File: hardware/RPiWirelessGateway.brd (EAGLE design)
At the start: 49.5 x 49.5 mm, 55 parts, among them IC1 MCP1702-3.3, X1 P1A, X2 CONN-SMATHD-SMD-EDGE, X3 P1B, X4 AVR ISP, X5 RPI FTDI

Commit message: Adding resistor to XBee TX line to protect if FTDI also fitted simultaneously.
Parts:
- added R3: 2k2, SteveMarple:RES-AXIAL-0.4
- R1: value 100k -> 1k
- R2: value 1k -> 100k
- RF2: value XRFB1 -> XRF
- X2: value CONN-SMATHD-SMD-EDGE -> SMA TH/EDGE
- moved R1 31.4 mm to (34.3, 34.3), turned to 180 degrees
- moved R2 31.4 mm to (17.8, 7.62), turned to 270 degrees
- moved U$24 24.8 mm to (21.0, 25.4), turned to 180 degrees
- moved U$11 24.8 mm to (5.08, 34.3), turned to 0 degrees
- moved U$17 22.9 mm to (5.08, 39.4), turned to 0 degrees
- moved U$25 21.6 mm to (5.71, 25.4), turned to 180 degrees
- moved U$21 19.6 mm to (21.0, 22.9), turned to 180 degrees
- moved U$14 19.1 mm to (5.08, 36.8), turned to 0 degrees
- moved U$22 19.1 mm to (5.71, 22.9), turned to 180 degrees
- moved U$20 16.5 mm to (5.08, 41.9), turned to 0 degrees
- moved U$19 16.1 mm to (5.71, 20.3)
- moved U$13 15.5 mm to (5.71, 15.2)
- moved U$18 15.5 mm to (21.0, 20.3)
- moved U$12 15.2 mm to (21.0, 15.2)
- moved U$26 10.2 mm to (5.08, 47.0)
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- renumbered XRF1 to RF2
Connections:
- new net N$42: R3.P$2, RF2.2, U$3.1
- net !XRF_RESET: now also R2.P$1; no longer R1.P$1
- net +3V3: now also R2.P$2; no longer R1.P$2
- net GND: now also U$24.1, U$26.1; no longer U$19.1, U$25.1
- net N$10: now also U$22.1; no longer U$18.1
- net N$11: now also U$19.1; no longer U$16.1
- net N$12: now also U$16.1; no longer U$14.1
- net N$13: now also U$13.1; no longer U$12.1
- net N$24: now also R1.P$2; no longer R2.P$2
- net N$30: now also U$23.1; no longer U$24.1
- net N$31: now also U$20.1; no longer U$22.1
- net N$38: now also R1.P$1; no longer R2.P$1
- net N$40: now also U$11.1; no longer U$21.1
- net N$5: now also U$12.1; no longer U$11.1
- net N$6: now also U$15.1; no longer U$13.1
- net N$7: now also U$18.1; no longer U$15.1
- net N$8: now also U$21.1; no longer U$17.1
- net N$9: now also U$25.1; no longer U$20.1
- net RX: now also U$17.1; no longer U$23.1
- net TX: now also R3.P$1, U$14.1; no longer RF2.2, U$26.1, U$3.1
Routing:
- net N$42: track 0.00 -> 12.8 mm
- net TX: track 72.4 -> 62.9 mm
- net RX: track 79.3 -> 84.2 mm
- net N$21: track 15.6 -> 12.6 mm
- net GND: track 149.9 -> 147.3 mm
- net N$22: track 10.8 -> 9.33 mm
- net N$9: track 7.85 -> 6.36 mm
- net N$20: track 10.3 -> 9.53 mm
- net P1-13: track 21.7 -> 22.4 mm
- net +3V3: track 104.6 -> 103.9 mm
- net N$41: track 17.7 -> 17.2 mm
- removed copper zone on layer 1, net +3V3

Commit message: Adding FET for open-drain control of AVR /RESET
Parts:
- added PAD_RFM12B_!INT!/VDI1, PAD_RFM12B_!INT!/VDI2: PAD, SteveMarple:PAD
- added Q1: 2N7000, SteveMarple:TO-92
- added R4: 2k2, SteveMarple:RES-AXIAL-0.4
- R1: value 1k -> 100k
- R3: value 2k2 -> 100k
- X4: device adafruit:AVRISP -> SteveMarple:CONN-HARTING-ML6
- moved U$11 24.8 mm to (21.0, 15.2), turned to 180 degrees
- moved U$15 22.9 mm to (5.08, 34.3), turned to 0 degrees
- moved U$18 22.9 mm to (5.08, 36.8), turned to 0 degrees
- moved U$21 22.9 mm to (5.08, 39.4), turned to 0 degrees
- moved U$24 22.9 mm to (5.08, 41.9), turned to 0 degrees
- moved PAD_RFM12B_FSK/DATA/!FFS 22.6 mm to (38.1, 8.89)
- moved R1 20.8 mm to (17.8, 21.6), turned to 90 degrees
- moved U$23 19.1 mm to (5.71, 25.4), turned to 180 degrees
- moved U$25 19.1 mm to (5.08, 44.5), turned to 0 degrees
- moved U$14 19.1 mm to (5.71, 17.8), turned to 180 degrees
- moved U$17 19.1 mm to (5.71, 20.3), turned to 180 degrees
- moved U$20 19.1 mm to (5.71, 22.9), turned to 180 degrees
- moved U$13 15.5 mm to (21.0, 17.8)
- moved U$16 15.5 mm to (21.0, 20.3)
- moved U$19 15.5 mm to (21.0, 22.9)
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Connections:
- net !XRF_RESET: now also R3.P$1; no longer R2.P$1
- net +3V3: now also PAD_RFM12B_!INT!/VDI2.1, R3.P$2; no longer R2.P$2
- net GND: now also PAD_RFM12B_!INT!/VDI1.1, Q1.1, R2.P$1, U$22.1; no longer U$24.1
- net N$10: now also U$20.1; no longer U$22.1
- net N$11: now also U$17.1; no longer U$19.1
- net N$12: now also U$14.1; no longer U$16.1
- net N$13: now also U$12.1; no longer U$13.1
- net N$24: now also Q1.3, R1.P$1; no longer R1.P$2
- net N$30: now also U$25.1; no longer U$23.1
- net N$31: now also U$24.1; no longer U$20.1
- net N$38: now also Q1.2, R2.P$2; no longer R1.P$1
- net N$4: now also R1.P$2
- net N$40: now also U$15.1; no longer U$11.1
- net N$42: now also R4.P$2; no longer R3.P$2
- net N$5: now also U$11.1; no longer U$12.1
- net N$6: now also U$13.1; no longer U$15.1
- net N$7: now also U$16.1; no longer U$18.1
- net N$8: now also U$19.1; no longer U$21.1
- net N$9: now also U$23.1; no longer U$25.1
- net RX: now also R4.P$1, U$21.1; no longer RF2.3, U$17.1, U$5.1
- net TX: now also RF2.3, U$18.1, U$5.1; no longer R3.P$1, U$14.1
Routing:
- net N$38: track 4.86 -> 52.8 mm
- net GND: track 147.3 -> 193.5 mm
- net N$24: track 16.4 -> 49.1 mm
- net N$4: track 3.81 -> 24.4 mm
- net +3V3: track 103.9 -> 87.4 mm
- net RX: track 84.2 -> 69.0 mm
- net TX: track 62.9 -> 75.3 mm
- net N$20: track 9.53 -> 20.1 mm
- net P1-22: track 30.5 -> 20.4 mm
- net N$41: track 17.2 -> 7.40 mm
- net MISO: track 30.5 -> 36.4 mm
- net SCK: track 36.9 -> 42.0 mm, vias 0 -> 1
- net P1-18: track 19.4 -> 22.4 mm
- net N$21: track 12.6 -> 15.6 mm
- net MOSI: track 38.6 -> 41.0 mm
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- removed copper zone on layer 16, net GND
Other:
- board text added: "(C) Steve Marple 2012"
- board text added: ">DRAWING_NAME"
- board text added: ">LAST_DATE_TIME"
- board text added: "License: CC BY-SA 3.0"
- board text added: "SN:"
- board text added: "Wireless Gateway"
- board text added: "for Raspberry Pi"
- board text removed: "Add license, credits, contact, S/N space etc to silkscreen"

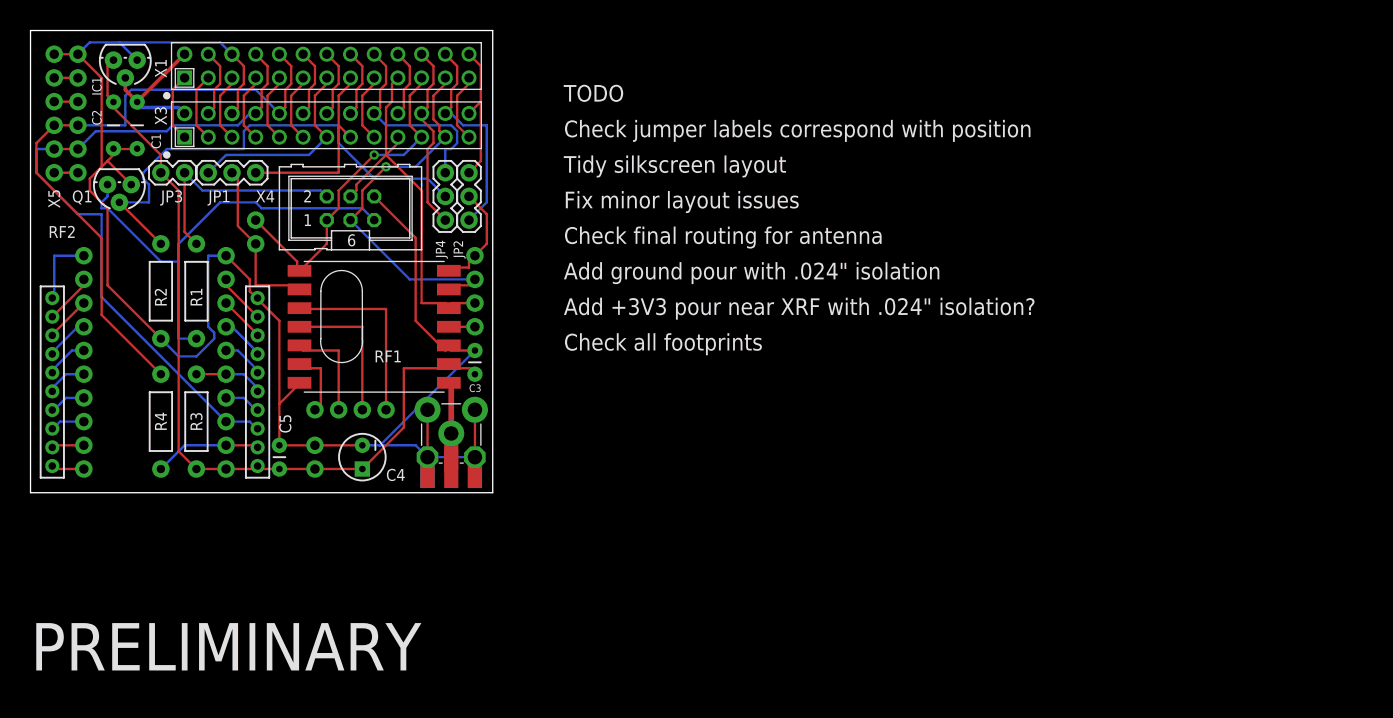
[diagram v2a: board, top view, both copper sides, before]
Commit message: Added optional pull-up for /FFS. Move breakout pads for XRF/XBee to allow Sparkfun XBee breakout board to be fitted.
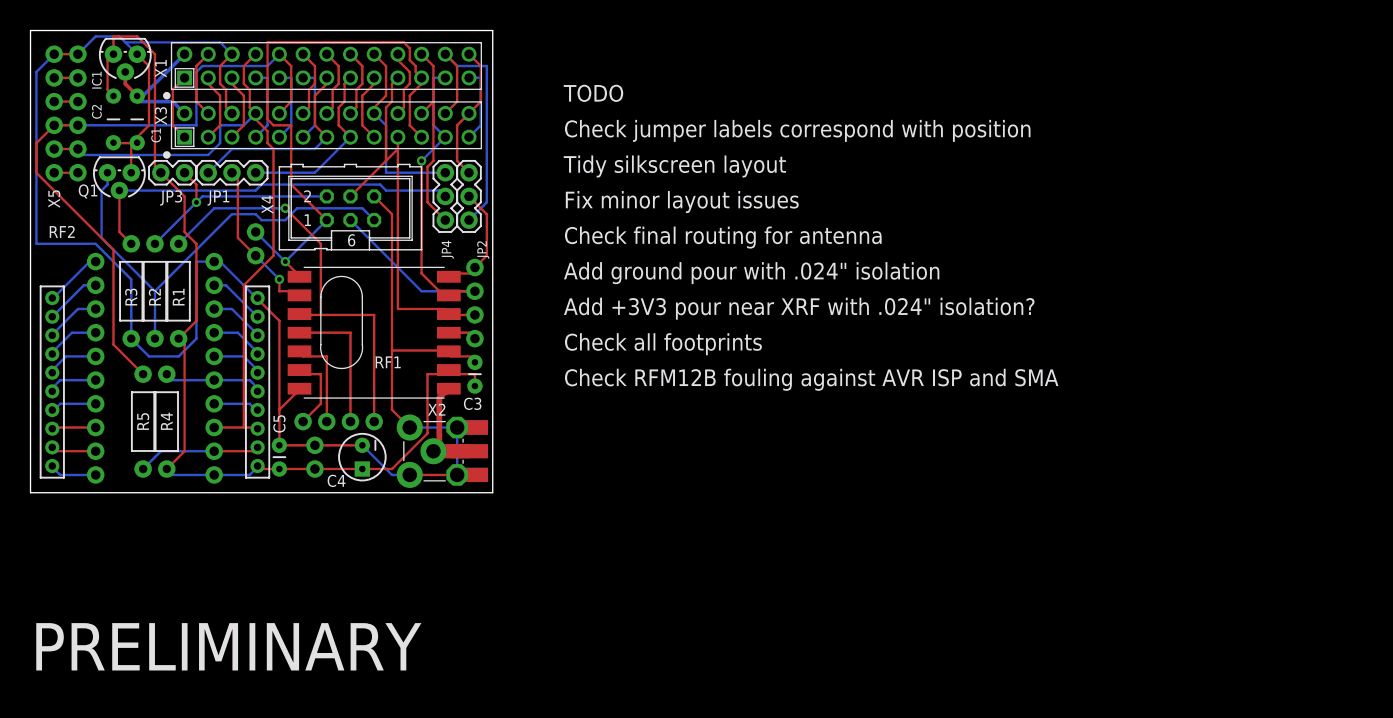
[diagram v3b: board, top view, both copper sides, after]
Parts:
- added R5: 2k2, SteveMarple:RES-AXIAL-0.4
- R4: value 2k2 -> 100k
- moved R3 15.6 mm to (10.8, 21.6), turned to 90 degrees
- moved X2 2.69 mm to (43.2, 4.45), turned to 90 degrees
- moved R1 1.91 mm to (15.9, 21.6), turned to 270 degrees
- moved PAD_RFM12B_CLK 1.80 mm to (31.8, 7.62)
- moved PAD_RFM12B_DCLK/CFIL/!FFS 1.80 mm to (34.3, 7.62)
- moved PAD_RFM12B_FSK/DATA/!FFS 1.80 mm to (36.8, 7.62)
- moved PAD_RFM12B_!RESET 1.80 mm to (29.2, 7.62)
- moved U$14 1.42 mm to (6.99, 17.1)
- moved U$17 1.42 mm to (6.99, 19.7)
- moved U$10 1.42 mm to (6.99, 12.1)
- moved U$12 1.42 mm to (6.99, 14.6)
- moved U$2 1.42 mm to (6.99, 1.91)
- moved U$4 1.42 mm to (6.99, 4.45)
- moved U$6 1.42 mm to (6.99, 6.99)
- moved U$8 1.42 mm to (6.99, 9.53)
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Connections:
- net !XRF_RESET: now also R4.P$1; no longer R3.P$1
- net +3V3: now also R1.P$2, R4.P$2; no longer R3.P$2
- net GND: now also R3.P$1; no longer R2.P$1
- net N$20: now also R1.P$1
- net N$24: now also R2.P$1; no longer R1.P$1
- net N$38: now also R3.P$2; no longer R2.P$2
- net N$4: now also R2.P$2; no longer R1.P$2
- net N$42: now also R5.P$2; no longer R4.P$2
- net RX: now also R5.P$1; no longer R4.P$1
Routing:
- net MISO: track 36.4 -> 62.4 mm
- net N$20: track 20.1 -> 45.5 mm, vias 0 -> 1
- net +3V3: track 87.4 -> 103.8 mm
- net N$38: track 52.8 -> 42.0 mm
- net GND: track 193.5 -> 203.4 mm
- net P1-24: track 23.3 -> 29.7 mm
- net SCK: track 42.0 -> 47.4 mm
- net !XRF_RESET: track 7.48 -> 10.7 mm
- net TX: track 75.3 -> 72.7 mm
- net MOSI: track 41.0 -> 43.6 mm
- net P1-15: track 21.4 -> 19.1 mm
- net N$1: track 5.51 -> 7.39 mm
- net N$42: track 11.5 -> 13.3 mm
- net P1-18: track 22.4 -> 20.6 mm
- net N$9: track 7.85 -> 6.25 mm
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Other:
- board text added: "Check RFM12B fouling against AVR ISP and SMA"

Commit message: Removed pullup for /FFS (internal pullup present). New RFM12B footprint.
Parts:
- removed R5: 2k2, SteveMarple:RES-AXIAL-0.4
- R4: value 100k -> 2k2
- moved R3 14.7 mm to (15.2, 7.62), turned to 270 degrees
- moved R4 3.18 mm to (11.4, 7.62)
- moved R2 1.91 mm to (11.4, 21.6)
- moved C4 1.27 mm to (34.3, 3.81), turned to 0 degrees
- moved PAD_RFM12B_!INT!/VDI1 1.27 mm to (29.2, 5.08)
- moved PAD_RFM12B_!INT!/VDI2 1.27 mm to (29.2, 2.54)
- moved R1 0.63 mm to (15.2, 21.6), turned to 90 degrees
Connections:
- net !XRF_RESET: now also R3.P$1; no longer R4.P$1
- net +3V3: now also R3.P$2; no longer R1.P$2, R4.P$2
- net GND: now also R2.P$1; no longer R3.P$1
- net N$20: no longer R1.P$1
- net N$24: now also R1.P$1; no longer R2.P$1
- net N$38: now also R2.P$2; no longer R3.P$2
- net N$4: now also R1.P$2; no longer R2.P$2
- net N$42: now also R4.P$2; no longer R5.P$2
- net RX: now also R4.P$1; no longer R5.P$1
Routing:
- net GND: track 203.4 -> 171.2 mm, vias 0 -> 1
- net N$20: track 45.5 -> 19.4 mm, vias 1 -> 0
- net N$24: track 48.6 -> 54.9 mm
- net MISO: track 62.4 -> 64.8 mm, vias 1 -> 0
- net +3V3: track 103.8 -> 101.5 mm
- net MOSI: track 43.6 -> 41.7 mm
- net N$42: track 13.3 -> 14.0 mm
- net !XRF_RESET: track 10.7 -> 10.0 mm
- net N$4: track 24.2 -> 23.6 mm
